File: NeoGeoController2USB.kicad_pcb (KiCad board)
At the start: 2 copper layers, 12 parts, among them CON1 AVR-ISP6, J1 USB, J2 DB15, U1 ATMEGA32U2-AU, X1 16Mhz

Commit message: First version fo the pcb.
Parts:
- added C5: 100nf, SM0603_Capa, F.Cu at (204.6, 152.4)
- R3: value 12K -> 10K
- moved CON1 163.2 mm to (197.4, 142.9), turned to 90 degrees
- moved X1 162.7 mm to (220.9, 146.1)
- moved C1 161.6 mm to (225.8, 148.6)
- moved C2 161.6 mm to (225.8, 143.5)
- moved C3 161.2 mm to (215.1, 152.4), turned to 90 degrees
- moved R2 160.9 mm to (209.8, 152.4)
- moved J2 160.4 mm to (210.6, 132.1)
- moved R1 160.4 mm to (211.8, 152.4)
- moved U1 160.4 mm to (210.6, 143.5)
- moved C4 160.4 mm to (206.8, 152.4)
- moved J1 160.0 mm to (210.6, 161.8)
- moved R3 151.6 mm to (202.1, 139.6)
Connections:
- U1 pad 10: A_BUTTON -> B_BUTTON
- U1 pad 11: B_BUTTON -> C_BUTTON
- U1 pad 12: C_BUTTON -> D_BUTTON
- U1 pad 13: D_BUTTON -> START
- U1 pad 14: START -> SELECT
- U1 pad 18: SELECT -> KICK_1
- U1 pad 19: KICK_3 -> D_KICK_2
- U1 pad 20: KICK_1 -> KICK_3
- U1 pad 21: D_KICK_2 -> (no net)
- U1 pad 5: (no net) -> UP
- U1 pad 6: UP -> DOWN
- U1 pad 7: DOWN -> LEFT
- U1 pad 8: LEFT -> RIGHT
- U1 pad 9: RIGHT -> A_BUTTON
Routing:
- net VCC: track 66.8 -> 126.7 mm
- net KICK_3: track 14.0 -> 43.3 mm
- net GND: track 94.1 -> 65.6 mm
- net SCK: track 0.00 -> 24.8 mm
- net KICK_1: track 12.4 -> 37.1 mm
- net D_KICK_2: track 16.0 -> 37.7 mm
- net MOSI: track 0.00 -> 16.2 mm
- net MISO: track 0.00 -> 12.2 mm
- net RESET: track 15.6 -> 24.9 mm
- net N-0000029: track 15.0 -> 10.5 mm
- net SELECT: track 10.6 -> 6.66 mm
- net LEFT: track 10.2 -> 12.6 mm
- net RIGHT: track 5.95 -> 7.64 mm
- net N-0000028: track 11.7 -> 10.6 mm
- net DOWN: track 9.82 -> 10.8 mm
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- added copper zone on B.Cu, net GND
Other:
- board outline added: 39.6 x 45.3 mm
- board text added: "Copyright 2014 antoine terrienne"
- board text added: "NeoGeoControllerToUSB v1.0"
- board text added: "https://github.com/letoine/NeoGeoControllerToUSB"

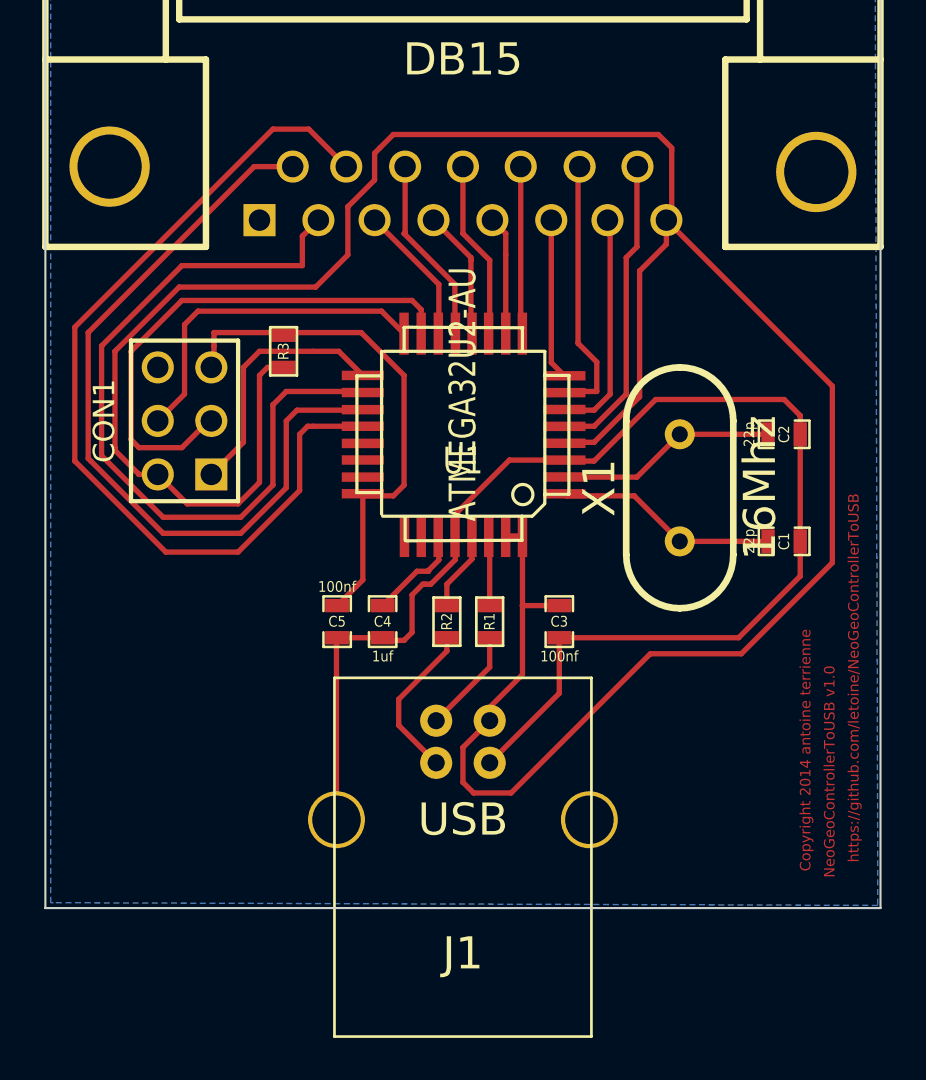
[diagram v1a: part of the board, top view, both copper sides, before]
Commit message: Shrinking board.
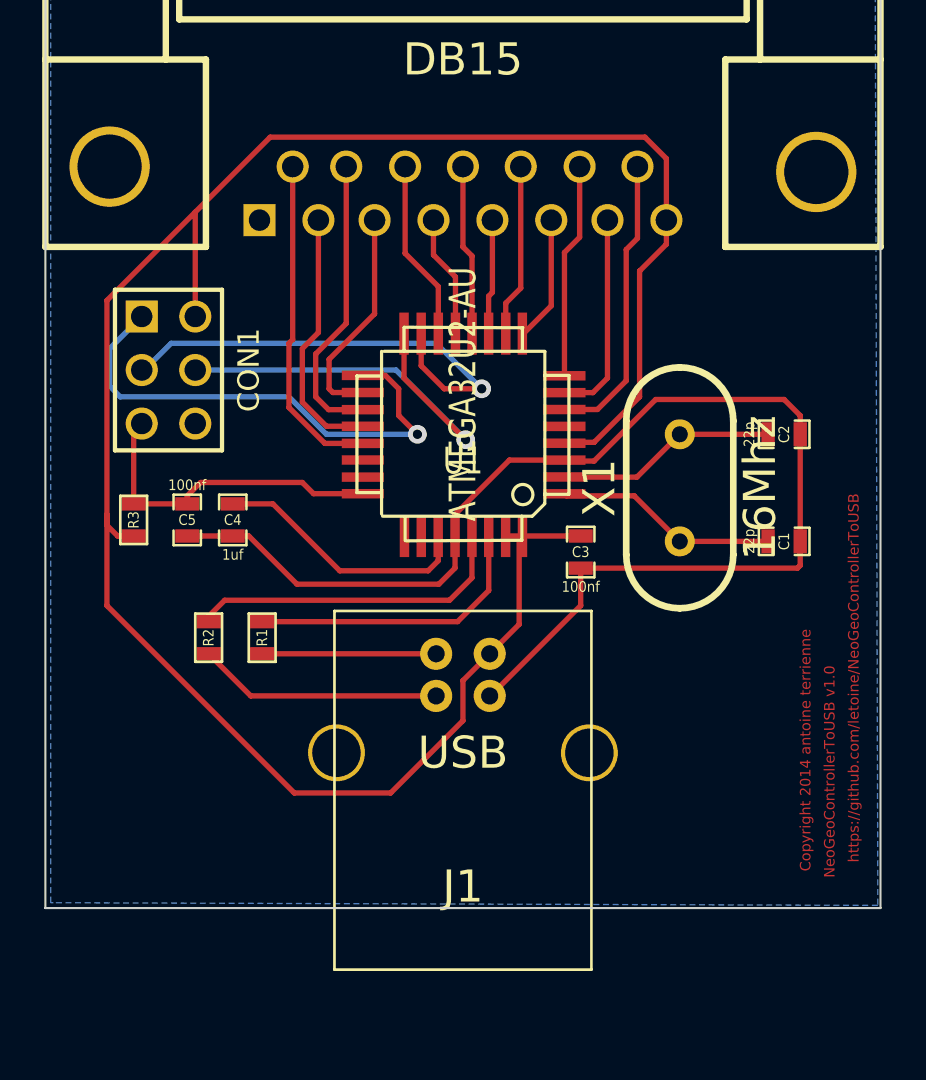
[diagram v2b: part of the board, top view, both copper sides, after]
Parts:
- moved R2 11.3 mm to (198.5, 153.2)
- moved R1 10.8 mm to (201.0, 153.2)
- moved R3 10.7 mm to (194.9, 147.6)
- moved C4 8.59 mm to (199.6, 147.6)
- moved C5 8.59 mm to (197.5, 147.6)
- moved C3 3.45 mm to (216.2, 149.1)
- moved J1 3.18 mm to (210.6, 158.6)
- moved CON1 2.53 mm to (196.6, 140.5), turned to 270 degrees
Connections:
- U1 pad 10: B_BUTTON -> A_BUTTON
- U1 pad 11: C_BUTTON -> B_BUTTON
- U1 pad 12: D_BUTTON -> C_BUTTON
- U1 pad 13: START -> D_BUTTON
- U1 pad 14: SELECT -> START
- U1 pad 18: KICK_1 -> SELECT
- U1 pad 19: D_KICK_2 -> KICK_3
- U1 pad 20: KICK_3 -> KICK_1
- U1 pad 21: (no net) -> D_KICK_2
- U1 pad 5: UP -> (no net)
- U1 pad 6: DOWN -> UP
- U1 pad 7: LEFT -> DOWN
- U1 pad 8: RIGHT -> LEFT
- U1 pad 9: A_BUTTON -> RIGHT
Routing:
- net KICK_3: track 43.3 -> 14.0 mm
- net KICK_1: track 37.1 -> 12.3 mm
- net VCC: track 126.7 -> 103.4 mm
- net D_KICK_2: track 37.7 -> 15.7 mm
- net MISO: track 12.2 -> 24.0 mm, vias 0 -> 1
- net N-0000027: track 3.79 -> 15.5 mm
- net N-0000016: track 3.32 -> 13.9 mm
- net RESET: track 24.9 -> 15.7 mm
- net N-0000015: track 4.74 -> 12.4 mm
- net GND: track 65.6 -> 61.0 mm
- net MOSI: track 16.2 -> 20.4 mm, vias 0 -> 1
- net N-0000023: track 7.62 -> 11.6 mm
- net SELECT: track 6.66 -> 10.6 mm
- net N-0000022: track 4.99 -> 8.25 mm
- net LEFT: track 12.6 -> 10.2 mm
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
